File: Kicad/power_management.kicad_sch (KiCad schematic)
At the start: 28 parts, among them U4 BQ25896RTWR, U5 BQ27220YZFR

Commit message: Feat: Added power LEDs 5v and 3v, Added Jumpers to battery and bms, Added segmentation in connector sheet, Added encoders, Changed page name from motor diver right to motor driver, Redid annotations, Changed output organisation on stm to match new ioc
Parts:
- added D3: RED_LED_5V, LED_SMD:LED_Cree-XHP50_3V_HighDensity, symbol Device:LED
- added D4: RED_LED_3v3, LED_SMD:LED_Cree-XHP50_3V_HighDensity, symbol Device:LED
- added R15: 1k, Button_Switch_THT:SW_NKK_GW12LJP, symbol Device:R_Small
- added R16: 470, Button_Switch_THT:SW_NKK_GW12LJP, symbol Device:R_Small
- renumbered C16 to C10, C17 to C11, C18 to C12, C6 to C13, C5 to C14, C4 to C15, C11 to C5, C12 to C6, C13 to C7, C14 to C8, C15 to C9, D3 to D1, D4 to D2, L2 to L1, R16 to R10, R19 to R11, R17 to R12, R18 to R13, R2 to R14, R4 to R17, R3 to R18, R11 to R5, R12 to R6, R13 to R7, R14 to R8, R15 to R9, U4 to U3, U5 to U4
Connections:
- net +3.3V: now also D4.2 (A)
- net +5V: now also D3.2 (A)
- net GND: now also R15.2, R16.2
- new net: D4.1 (K), R16.1
- new net: D3.1 (K), R15.1
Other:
- moved on the sheet: C13, C14, C15, R14, R17, R18, U4

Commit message: feat: added the footprints for the solderjumpers
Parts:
- R18: footprint Resistor_SMD:R_0402_1005Metric -> Resistor_SMD:R_2512_6332Metric
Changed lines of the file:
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@@
 			)
 		)
-		(property "Footprint" "Resistor_SMD:R_0402_1005Metric"
+		(property "Footprint" "Resistor_SMD:R_2512_6332Metric"
 			(at 237.49 68.58 0)
 			(hide yes)

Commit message: fix: assigned the correct footprints to resistors R15 and R16
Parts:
- R15, R16: footprint Button_Switch_THT:SW_NKK_GW12LJP -> Resistor_SMD:R_0402_1005Metric
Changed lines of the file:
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@@
 			)
 		)
-		(property "Footprint" "Button_Switch_THT:SW_NKK_GW12LJP"
+		(property "Footprint" "Resistor_SMD:R_0402_1005Metric"
 			(at 222.25 119.38 0)
 			(hide yes)
@@
 			)
 		)
-		(property "Footprint" "Button_Switch_THT:SW_NKK_GW12LJP"
+		(property "Footprint" "Resistor_SMD:R_0402_1005Metric"
 			(at 200.66 119.38 0)
 			(hide yes)

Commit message: feat: changed the footprints to 1206 for the shunt resistors R18 and R19 and put a JST connector footprint for the Bluetooth Module
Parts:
- R18: footprint Resistor_SMD:R_2512_6332Metric -> Resistor_SMD:R_1206_3216Metric
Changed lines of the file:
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@@
 			)
 		)
-		(property "Footprint" "Resistor_SMD:R_2512_6332Metric"
+		(property "Footprint" "Resistor_SMD:R_1206_3216Metric"
 			(at 237.49 68.58 0)
 			(hide yes)

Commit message: feat: electrical schematic validated
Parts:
- removed R11: 10k, Resistor_SMD:R_0402_1005Metric, symbol Device:R_Small_US
- added C3, C4: 1u, Capacitor_SMD:C_0402_1005Metric, symbol Device:C_Small
- added J14: USB_C_Receptacle_USB2.0_16P, Connector_USB:USB_C_Receptacle_GCT_USB4105-xx-A_16P_TopMnt_Horizontal, symbol Connector:USB_C_Receptacle_USB2.0_16P
- added J2: Connecteur batterie, Connector_JST:JST_XH_B2B-XH-A_1x02_P2.50mm_Vertical, symbol Connector:Conn_01x02_Pin
- added JP1: JMP_LDO_In, Jumper:SolderJumper-2_P1.3mm_Open_TrianglePad1.0x1.5mm, symbol Jumper:SolderJumper_2_Open
- added JP2: JMP_LDO_Out, Jumper:SolderJumper-2_P1.3mm_Open_TrianglePad1.0x1.5mm, symbol Jumper:SolderJumper_2_Open
- added JP4, JP5: JMP_Battery, Jumper:SolderJumper-2_P1.3mm_Open_TrianglePad1.0x1.5mm, symbol Jumper:SolderJumper_2_Open
- added Q1: DMP1045UQ-7, DMP1045UQ-7_DIO, symbol DMP1045UQ-7:DMP1045UQ-7
- added R1, R3: 10k, Resistor_SMD:R_0402_1005Metric, symbol Device:R
- added R11, R4: 100k, Resistor_SMD:R_0402_1005Metric, symbol Device:R
- added R2: 100, Resistor_SMD:R_0402_1005Metric, symbol Device:R
- added R20, R21: 5k1, Resistor_SMD:R_0402_1005Metric, symbol Device:R_Small
- added U2: LD39050PU33R, footprints_LD39:DFN6_3X3_STM, symbol LD39050PU33R:LD39050PU33R
- added U6: USBLC6-2SC6, Package_TO_SOT_SMD:SOT-23-6, symbol Power_Protection:USBLC6-2SC6
- added U7: DMN313DLT-7, SOT-523_DIO, symbol DMN313DLT:DMN313DLT-7
- added U8: MMDT2907A-7-F, SOT-363_DIO, symbol MMDT2907A-7-F:MMDT2907A-7-F
- C10, C11, C12, C6, C9: value 10µF -> 10u/25V
- C13: value 470nF -> 470n; footprint Capacitor_SMD:C_0603_1608Metric -> Capacitor_SMD:C_0402_1005Metric
- C14: value 2.2µF -> 2u2; footprint Capacitor_SMD:C_0603_1608Metric -> Capacitor_SMD:C_0402_1005Metric
- C15, C5: value 1µF -> 1u
- C7: value 47nF -> 47n; footprint Capacitor_SMD:C_0603_1608Metric -> Capacitor_SMD:C_0402_1005Metric
- C8: value 4.7µF -> 4u7
- D3, D4: footprint LED_SMD:LED_Cree-XHP50_3V_HighDensity -> LED_SMD:LED_0603_1608Metric
- L1: value 1µH -> 1u
- R10, R9: value 2.2k -> 2k2
- R12: value 5.23k -> 10k
- R13: value 30.1k -> 10k
- R16, R6: value 470 -> 470R
- R5, R7: value 1.5k -> 1k5
- R8: value 4.7k -> 4k7
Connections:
- net +3.3V: now also JP2.2 (B); no longer D4.2 (A), R14.1, R5.1, R7.1, R8.1
- net +5V: now also JP5.2 (B), Q1.2, U8.1 (E2); no longer C5.2, U3.1 (VBUS)
- net BAT: now also J2.1 (Pin_1)
- net GND: now also C3.2, C4.2, J14.A1 (GND), J14.A12 (GND), J14.B1 (GND), J14.B12 (GND), J14.S1 (SHIELD), J2.2 (Pin_2), R11.2, R20.2, R21.1, R3.1, R4.2, U2.2 (GND), U2.7 (GND), U6.2 (GND), U7.1 (G)
- net OTG_EN: no longer names the net of U3.8 (OTG_IUSB)
- net OTG_EN: now also R1.2, U7.2 (S)
- net SYS renamed VCC
- net VCC: now also JP1.2 (B), R1.1
- new net: C5.2, JP5.1 (A), U3.1 (VBUS)
- new net: C3.1, JP1.1 (A), U2.1 (EN), U2.6 (VIN)
- new net: C4.1, JP2.1 (A), U2.4 (VOUT)
- new net: R2.2, R3.2, U7.3 (D)
- new net: J14.A4 (VBUS), J14.A9 (VBUS), J14.B4 (VBUS), J14.B9 (VBUS), JP4.1 (A)
- new net: Q1.1, R11.1, U8.6 (C2)
- new net: J14.B5 (CC2), R21.2
- new net: J14.A5 (CC1), R20.1
- new net: R4.1, U8.2 (B2), U8.3 (C1), U8.5 (B1)
- new net +3V3: D4.2 (A), R14.1, R5.1, R7.1, R8.1
- new net D+: J14.A6 (D+), J14.B6 (D+), U6.3 (I/O2)
- new net D-: J14.A7 (D-), J14.B7 (D-), U6.1 (I/O1)
- new net USB_DM: U6.6 (I/O1)
- new net USB_DP: U6.4 (I/O2)
- new net VBUS: JP4.2 (B), Q1.3, R2.1, U6.5 (VBUS), U8.4 (E1)
- no-connect marks 2 -> 5
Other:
- note added: "->"
- note added: "SYS"
- moved on the sheet: C13, C14, C15, C5, D3, D4, R14, R15, R16, R17, R18, U4

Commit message: feat: added the footprints for new components and started assigning the JLCPCB part numbers
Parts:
- C10, C11, C12, C6, C9: JLCPCB Part # (none) -> C96446
- C13: footprint Capacitor_SMD:C_0402_1005Metric -> Capacitor_SMD:C_0603_1608Metric; JLCPCB Part # (none) -> C1623
- C14: JLCPCB Part # (none) -> C12530
- C15, C3, C4, C5: JLCPCB Part # (none) -> C52923
- C7: footprint Capacitor_SMD:C_0402_1005Metric -> Capacitor_SMD:C_0603_1608Metric; JLCPCB Part # (none) -> C1622
- C8: JLCPCB Part # (none) -> C23733
- D1, D2, D4: JLCPCB Part # (none) -> C965804
- D3: footprint LED_SMD:LED_0603_1608Metric -> LED_THT:LED_D5.0mm_FlatTop; JLCPCB Part # (none) -> C5756798
- L1: footprint Inductor_SMD:L_Coilcraft_XxL4020 -> Inductor_SMD:L_Sunlord_SWPA4030S
- Q1: footprint DMP1045UQ-7_DIO -> footprints_DMP:DMP1045UQ-7_DIO
- U7: footprint SOT-523_DIO -> footprints_DMN:SOT-523_DIO
- U8: footprint SOT-363_DIO -> footprints_MMDT:SOT-363_DIO
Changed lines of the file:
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@@
 			)
 		)
+		(property "JLCPCB Part #" "C96446"
+			(at 54.61 39.37 90)
+			(hide yes)
+			(show_name no)
+			(do_not_autoplace no)
+			(effects
+				(font
+					(size 1.27 1.27)
+				)
+			)
+		)
 		(pin "1"
 		)
@@
 			)
 		)
+		(property "JLCPCB Part #" "C96446"
+			(at 133.35 35.56 0)
+			(hide yes)
+			(show_name no)
+			(do_not_autoplace no)
+			(effects
+				(font
+					(size 1.27 1.27)
+				)
+			)
+		)
 		(pin "1"
 		)
@@
 			)
 		)
+		(property "JLCPCB Part #" "C52923"
+			(at 270.51 40.64 0)
+			(hide yes)
+			(show_name no)
+			(do_not_autoplace no)
+			(effects
+				(font
+					(size 1.27 1.27)
+				)
+			)
+		)
 		(pin "1"
 		)
@@
 			)
 		)
+		(property "JLCPCB Part #" "C965804"
+			(at 46.99 59.69 0)
+			(hide yes)
+			(show_name no)
+			(do_not_autoplace no)
+			(effects
+				(font
+					(size 1.27 1.27)
+				)
+			)
+		)
 		(pin "1"
 		)
@@
 			)
 		)
+		(property "JLCPCB Part #" "C965804"
+			(at 46.99 66.04 0)
+			(hide yes)
+			(show_name no)
+			(do_not_autoplace no)
+			(effects
+				(font
+					(size 1.27 1.27)
+				)
+			)
+		)
 		(pin "1"
 		)
@@
 			)
 		)
+		(property "JLCPCB Part #" "C96446"
+			(at 124.46 69.85 0)
+			(hide yes)
+			(show_name no)
+			(do_not_autoplace no)
+			(effects
+				(font
+					(size 1.27 1.27)
+				)
+			)
+		)
 		(pin "1"
 		)
@@
 			)
 		)
-		(property "Footprint" "DMP1045UQ-7_DIO"
+		(property "Footprint" "footprints_DMP:DMP1045UQ-7_DIO"
 			(at 165.1 132.08 0)
 			(hide yes)
@@
 			)
 		)
+		(property "JLCPCB Part #" "C52923"
+			(at 45.72 163.83 0)
+			(hide yes)
+			(show_name no)
+			(do_not_autoplace no)
+			(effects
+				(font
+					(size 1.27 1.27)
+				)
+			)
+		)
 		(pin "1"
 		)
@@
 			)
 		)
-		(property "Footprint" "Capacitor_SMD:C_0402_1005Metric"
+		(property "Footprint" "Capacitor_SMD:C_0603_1608Metric"
 			(at 190.5 57.15 0)
 			(hide yes)
@@
 			)
 		)
+		(property "JLCPCB Part #" "C1623"
+			(at 190.5 57.15 0)
+			(hide yes)
+			(show_name no)
+			(do_not_autoplace no)
+			(effects
+				(font
+					(size 1.27 1.27)
+				)
+			)
+		)
 		(pin "1"
 		)
@@
 			)
 		)
+		(property "JLCPCB Part #" "C52923"
+			(at 31.75 38.1 90)
+			(hide yes)
+			(show_name no)
+			(do_not_autoplace no)
+			(effects
+				(font
+					(size 1.27 1.27)
+				)
+			)
+		)
 		(pin "1"
 		)
@@
 			)
 		)
+		(property "JLCPCB Part #" "C965804"
+			(at 265.43 82.55 90)
+			(hide yes)
+			(show_name no)
+			(do_not_autoplace no)
+			(effects
+				(font
+					(size 1.27 1.27)
+				)
+			)
+		)
 		(pin "2"
 		)
@@
 			)
 		)
-		(property "Footprint" "Capacitor_SMD:C_0402_1005Metric"
+		(property "Footprint" "Capacitor_SMD:C_0603_1608Metric"
 			(at 101.9048 31.75 0)
 			(hide yes)
@@
 			)
 		)
+		(property "JLCPCB Part #" "C1622"
+			(at 102.87 35.56 0)
+			(hide yes)
+			(show_name no)
+			(do_not_autoplace no)
+			(effects
+				(font
+					(size 1.27 1.27)
+				)
+			)
+		)
 		(pin "1"
 		)
@@
 			)
 		)
+		(property "JLCPCB Part #" "C12530"
+			(at 198.12 57.15 0)
+			(hide yes)
+			(show_name no)
+			(do_not_autoplace no)
+			(effects
+				(font
+					(size 1.27 1.27)
+				)
+			)
+		)
 		(pin "2"
 		)
@@
 			)
 		)
-		(property "Footprint" "SOT-523_DIO"
+		(property "Footprint" "footprints_DMN:SOT-523_DIO"
 			(at 50.8 127 0)
 			(hide yes)
@@
 			)
 		)
+		(property "JLCPCB Part #" "C96446"
+			(at 114.3 69.85 0)
+			(hide yes)
+			(show_name no)
+			(do_not_autoplace no)
+			(effects
+				(font
+					(size 1.27 1.27)
+				)
+			)
+		)
 		(pin "1"
 		)
@@
 			)
 		)
-		(property "Footprint" "Inductor_SMD:L_Coilcraft_XxL4020"
+		(property "Footprint" "Inductor_SMD:L_Sunlord_SWPA4030S"
 			(at 113.03 31.75 0)
 			(hide yes)
@@
 			)
 		)
+		(property "JLCPCB Part #" "C23733"
+			(at 109.22 48.26 0)
+			(hide yes)
+			(show_name no)
+			(do_not_autoplace no)
+			(effects
+				(font
+					(size 1.27 1.27)
+				)
+			)
+		)
 		(pin "1"
 		)
@@
 			)
 		)
-		(property "Footprint" "SOT-363_DIO"
+		(property "Footprint" "footprints_MMDT:SOT-363_DIO"
 			(at 146.05 132.08 0)
 			(hide yes)
@@
 			)
 		)
+		(property "JLCPCB Part #" "C52923"
+			(at 105.41 170.18 0)
+			(hide yes)
+			(show_name no)
+			(do_not_autoplace no)
+			(effects
+				(font
+					(size 1.27 1.27)
+				)
+			)
+		)
 		(pin "2"
 		)
@@
 			)
 		)
-		(property "Footprint" "LED_SMD:LED_0603_1608Metric"
+		(property "Footprint" "LED_THT:LED_D5.0mm_FlatTop"
 			(at 243.84 82.55 0)
 			(hide yes)
@@
 			)
 		)
+		(property "JLCPCB Part #" "C5756798"
+			(at 243.84 82.55 90)
+			(hide yes)
+			(show_name no)
+			(do_not_autoplace no)
+			(effects
+				(font
+					(size 1.27 1.27)
+				)
+			)
+		)
 		(pin "2"
 		)
@@
 			(at 123.19 35.56 0)
 			(hide yes)
+			(show_name no)
+			(do_not_autoplace no)
+			(effects
+				(font
+					(size 1.27 1.27)
+				)
+			)
+		)
+		(property "JLCPCB Part #" "C96446"
+			(at 123.19 35.56 0)
+			(hide yes)

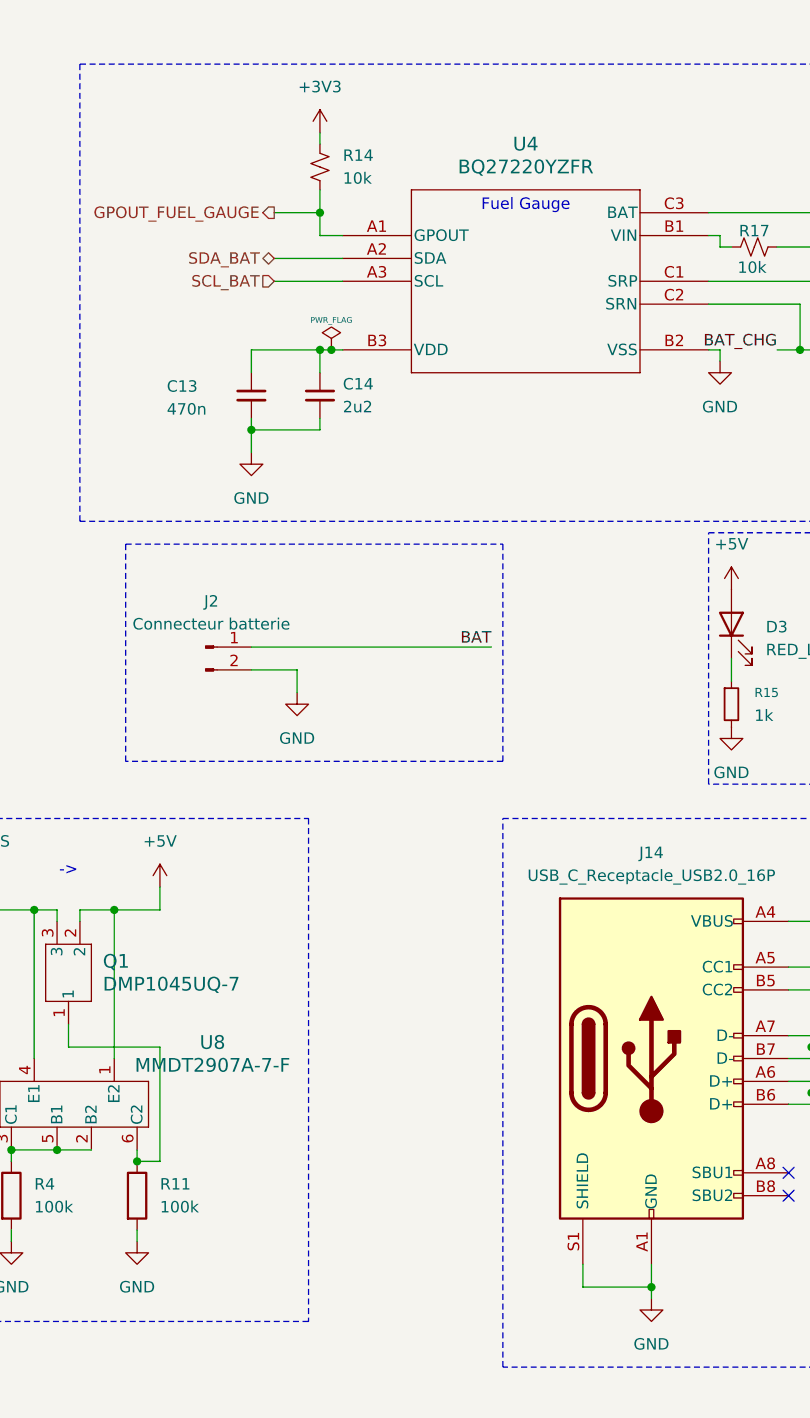
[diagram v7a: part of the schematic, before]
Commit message: Feat: Placed components on wiring schematic, chore: fixed footprint names and values
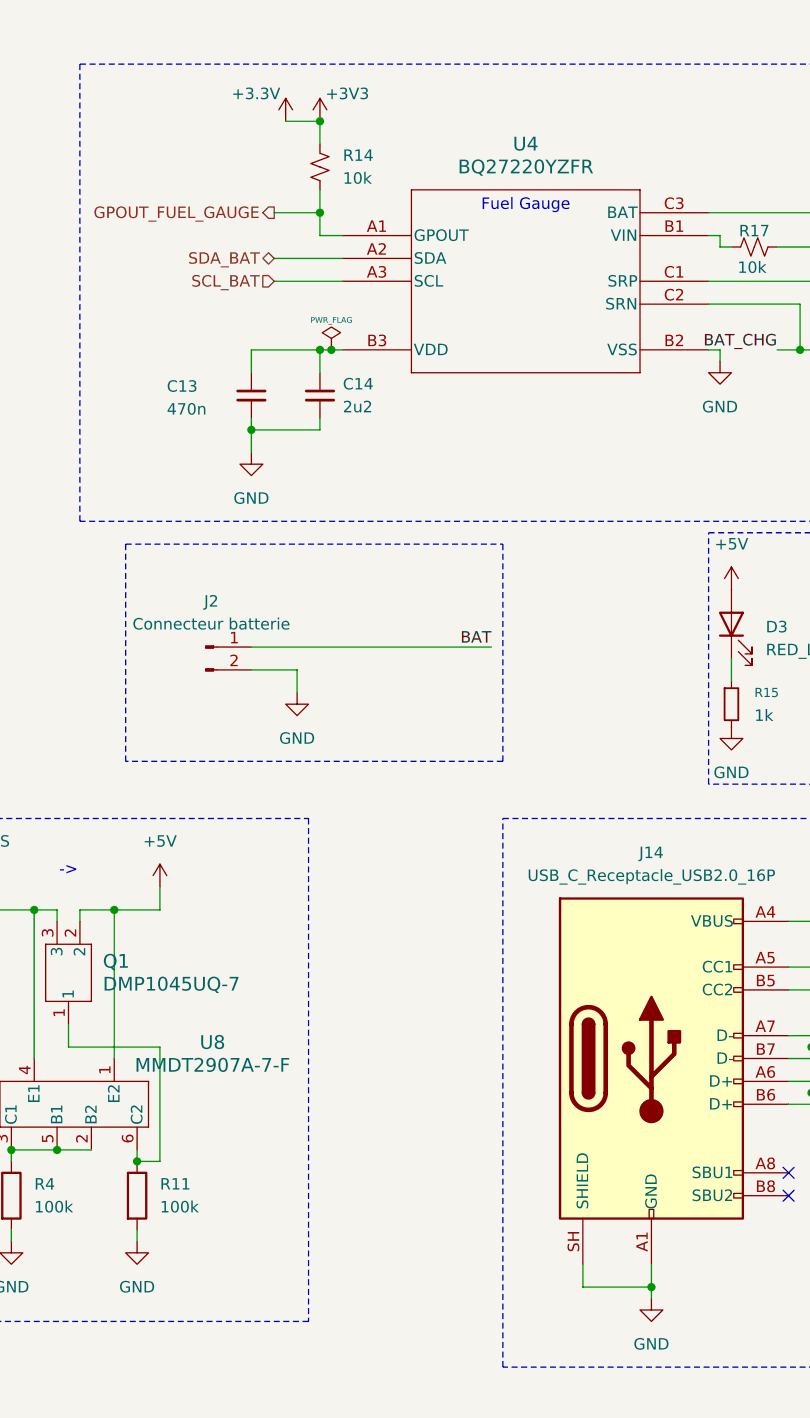
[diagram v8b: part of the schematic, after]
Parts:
- D3: footprint LED_THT:LED_D5.0mm_FlatTop -> LED_SMD:LED_0603_1608Metric
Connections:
- net +3V3 is gone; now on net +3.3V: D4.2 (A), R14.1, R5.1, R7.1, R8.1
- net GND: now also J14.SH (SHIELD); no longer J14.S1 (SHIELD)
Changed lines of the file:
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@@
 	)
 	(junction
+		(at 198.12 26.67)
+		(diameter 0)
+		(color 0 0 0 0)
+	)
+	(junction
 		(at 99.06 66.04)
 		(diameter 0)
@@
 	(wire
 		(pts
+			(xy 194.31 26.67) (xy 198.12 26.67)
+		)
+		(stroke
+			(width 0)
+			(type default)
+		)
+	)
+	(wire
+		(pts
 			(xy 190.5 85.09) (xy 217.17 85.09)
 		)
@@
 	(wire
 		(pts
+			(xy 198.12 26.67) (xy 198.12 29.21)
+		)
+		(stroke
+			(width 0)
+			(type default)
+		)
+	)
+	(wire
+		(pts
 			(xy 265.43 152.4) (xy 265.43 154.94)
 		)
@@
 	(wire
 		(pts
-			(xy 198.12 29.21) (xy 198.12 27.94)
-		)
-		(stroke
-			(width 0)
-			(type default)
-		)
-	)
-	(wire
-		(pts
 			(xy 254 120.65) (xy 254 119.38)
 		)
@@
 	(symbol
 		(lib_id "power:+3V3")
-		(at 198.12 27.94 0)
+		(at 198.12 26.67 0)
 		(unit 1)
 		(body_style 1)
@@
 		(in_pos_files yes)
 		(dnp no)
-		(fields_autoplaced yes)
 		(property "Reference" "#PWR053"
-			(at 198.12 31.75 0)
+			(at 198.12 30.48 0)
 			(hide yes)
 			(show_name no)
@@
 		)
 		(property "Value" "+3V3"
-			(at 198.12 22.86 0)
+			(at 201.168 23.622 0)
 			(show_name no)
 			(do_not_autoplace no)
@@
 		)
 		(property "Footprint" ""
-			(at 198.12 27.94 0)
+			(at 198.12 26.67 0)
 			(hide yes)
 			(show_name no)
@@
 		)
 		(property "Datasheet" ""
-			(at 198.12 27.94 0)
+			(at 198.12 26.67 0)
 			(hide yes)
 			(show_name no)
@@
 		)
 		(property "Description" "Power symbol creates a global label with name \"+3V3\""
-			(at 198.12 27.94 0)
+			(at 198.12 26.67 0)
 			(hide yes)
 			(show_name no)
@@
 		(pin "A6"
 		)
-		(pin "S1"
+		(pin "SH"
 		)
 		(instances
@@
 	)
 	(symbol
+		(lib_id "power:+3.3V")
+		(at 194.31 26.67 0)
+		(unit 1)
+		(body_style 1)
+		(exclude_from_sim no)
+		(in_bom yes)
+		(on_board yes)
+		(in_pos_files yes)
+		(dnp no)
+		(property "Reference" "#PWR049"
+			(at 194.31 30.48 0)
+			(hide yes)
+			(show_name no)
+			(do_not_autoplace no)
+			(effects
+				(font
+					(size 1.27 1.27)
+				)
+			)
+		)
+		(property "Value" "+3.3V"
+			(at 191.008 23.622 0)
+			(show_name no)
+			(do_not_autoplace no)
+			(effects
+				(font
+					(size 1.27 1.27)
+				)
+			)
+		)
+		(property "Footprint" ""
+			(at 194.31 26.67 0)
+			(hide yes)
+			(show_name no)
+			(do_not_autoplace no)
+			(effects
+				(font
+					(size 1.27 1.27)
+				)
+			)
+		)
+		(property "Datasheet" ""
+			(at 194.31 26.67 0)
+			(hide yes)
+			(show_name no)
+			(do_not_autoplace no)
+			(effects
+				(font
+					(size 1.27 1.27)
+				)
+			)
+		)
+		(property "Description" "Power symbol creates a global label with name \"+3.3V\""
+			(at 194.31 26.67 0)
+			(hide yes)
+			(show_name no)
+			(do_not_autoplace no)
+			(effects
+				(font
+					(size 1.27 1.27)
+				)
+			)
+		)
+		(pin "1"
+		)
+		(instances
+			(project "Redoubot"
+				(path "/43131b41-4104-4cd6-9c2f-4d5da1687300/73350c17-84ab-42d8-b086-6cfec23927e8"
+					(reference "#PWR049")
+					(unit 1)
+				)
+			)
+		)
+	)
+	(symbol
 		(lib_id "Device:L")
 		(at 113.03 31.75 90)
@@
 			)
 		)
-		(property "Footprint" "LED_THT:LED_D5.0mm_FlatTop"
+		(property "Footprint" "LED_SMD:LED_0603_1608Metric"
 			(at 243.84 82.55 0)
 			(hide yes)
